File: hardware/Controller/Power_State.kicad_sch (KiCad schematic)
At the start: 24 parts, among them J3 ICSP Header, J7 UART DEBUG, Q2 NMOS, SW1 Button - User Interface, SW2 Button - Reset, U4 ATmega328-P, Y2 16 Mhz

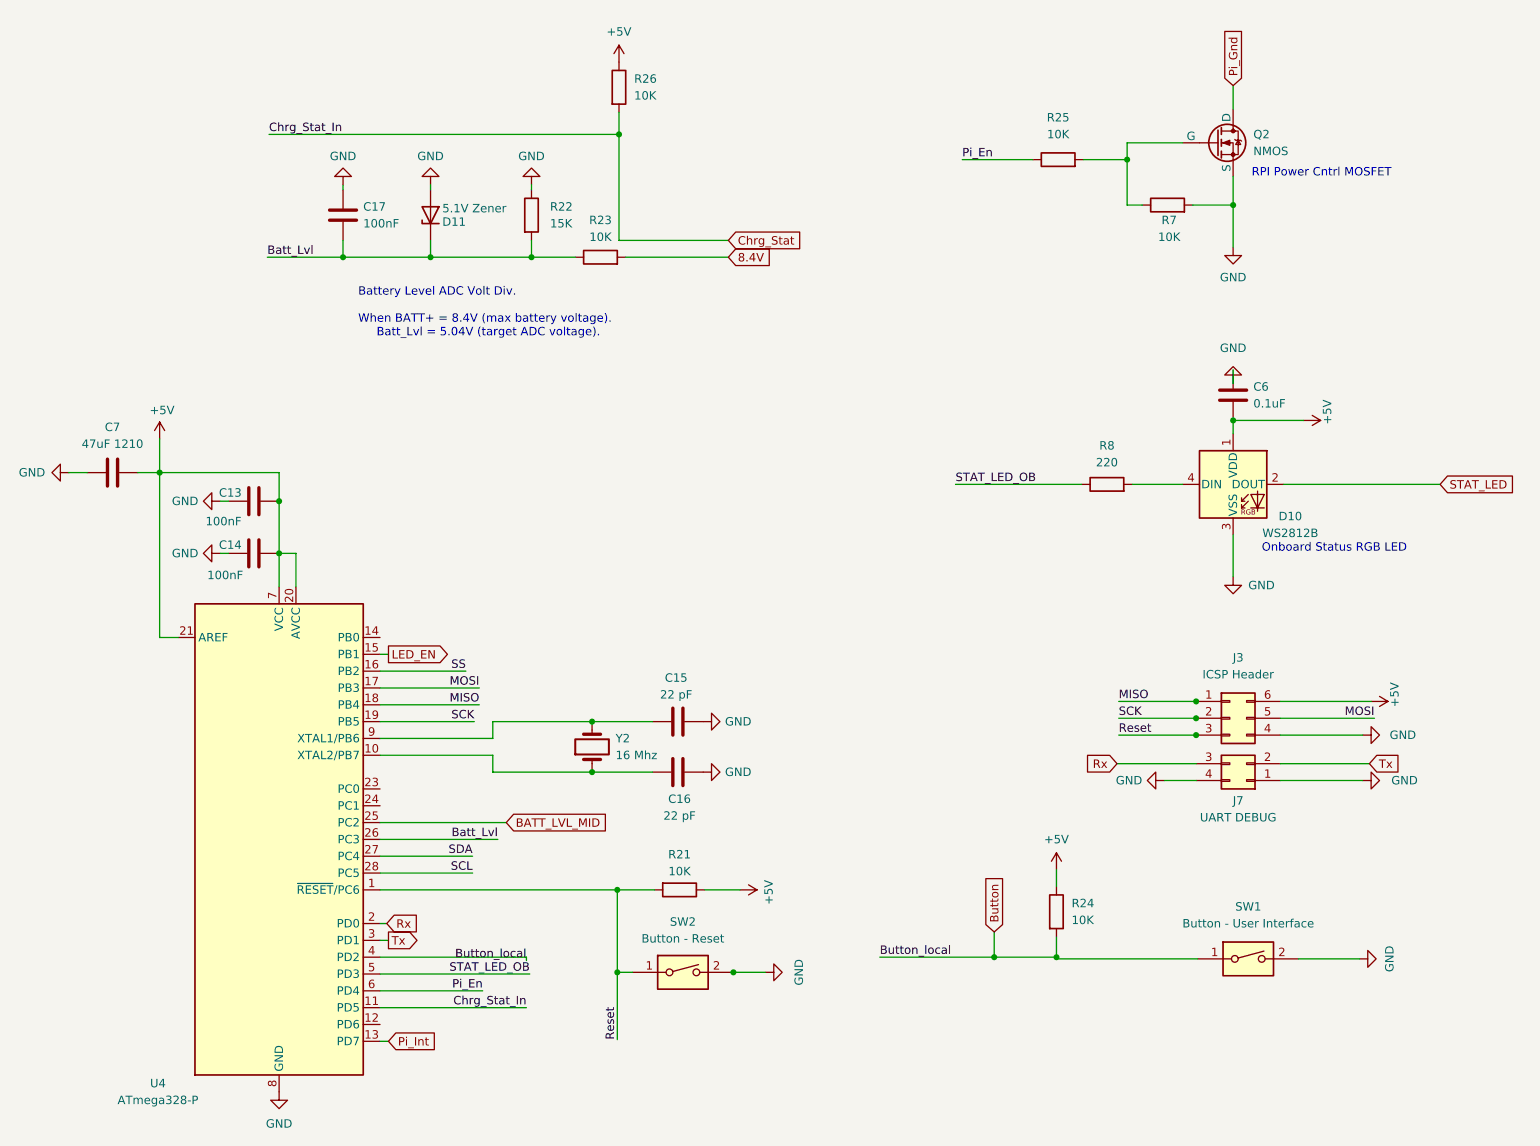
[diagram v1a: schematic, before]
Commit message: Hardware - Controller - Rev 0.3
* Consolidate various asset dirs into single symlinked directory.
* Fixes major flaw with previous atmega328 layout - wrong schematic symbol caused incorrect routing
* Use smaller crystal closer to mcu
* Add QR to silkscreen
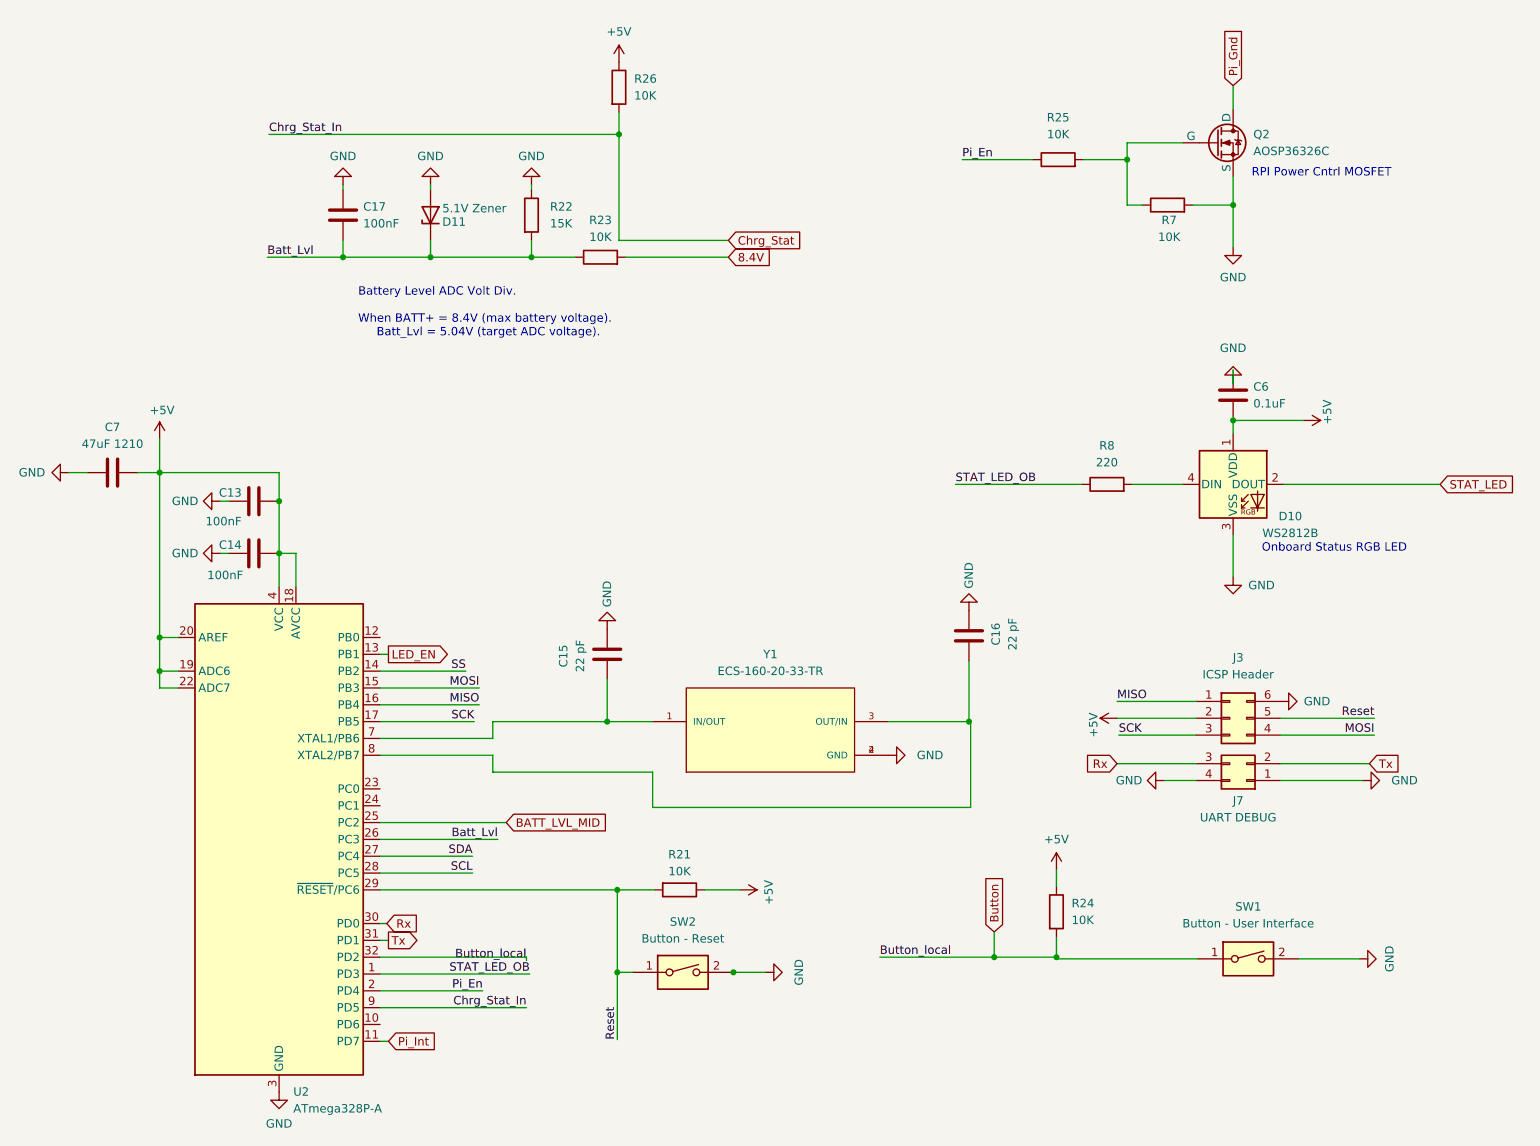
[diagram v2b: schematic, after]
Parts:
- removed U4: ATmega328-P, ATMEGA328-AU:QFP80P900X900X120-32N, symbol MCU_Microchip_ATmega:ATmega328-P
- removed Y2: 16 Mhz, Crystal - 16MHz ECS_160_20_5PX_TR:XTAL_ECS-160-20-5PX-TR, symbol Device:Crystal
- added U2: ATmega328P-A, Package_QFP:TQFP-32_7x7mm_P0.8mm, symbol MCU_Microchip_ATmega:ATmega328P-A
- added Y1: ECS-160-20-33-TR, ECS-160-20-33-TR:XTAL_ECS-160-20-33-TR, symbol ECS-160-20-33-TR:ECS-160-20-33-TR
- D11: footprint Diode_SMD:D_MiniMELF_Handsoldering -> Diode_SMD:D_SOD-323_HandSoldering
- Q2: value NMOS -> AOSP36326C; footprint FET - AOSP36326C:SOIC127P490X600X175-8N -> AOSP36326C:SOIC127P490X600X175-8N
- SW1, SW2: footprint Button - PTS815 Tactile SW:SW4_PTS815 SJM 250 SMTR LFS_CNK -> Button - PTS815:SW4_PTS815 SJM 250 SMTR LFS_CNK
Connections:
- net +5V: now also J3.2 (Pin_2), U2.18 (AVCC), U2.19 (ADC6), U2.20 (AREF), U2.22 (ADC7), U2.4 (VCC), U2.6 (VCC); no longer J3.6 (Pin_6)
- net BATT_LVL_MID: now also U2.25 (PC2)
- net Batt_Lvl: now also U2.26 (PC3)
- net Button: now also U2.32 (PD2)
- net Chrg_Stat: now also U2.9 (PD5)
- net GND: now also J3.6 (Pin_6), U2.21 (GND), U2.3 (GND), U2.5 (GND), Y1.2 (GND), Y1.4 (GND); no longer J3.4 (Pin_4)
- net LED_EN: now also U2.13 (PB1)
- net MISO: now also U2.16 (PB4)
- net MOSI: now also J3.4 (Pin_4), U2.15 (PB3); no longer J3.5 (Pin_5)
- net Pi_En: now also U2.2 (PD4)
- net Pi_Int: now also U2.11 (PD7)
- net Reset: now also J3.5 (Pin_5), U2.29 (~{RESET}/PC6); no longer J3.3 (Pin_3)
- net Rx: now also U2.30 (PD0)
- net SCK: now also J3.3 (Pin_3), U2.17 (PB5); no longer J3.2 (Pin_2)
- net SCL: now also U2.28 (PC5)
- net SDA: now also U2.27 (PC4)
- net SS: now also U2.14 (PB2)
- net STAT_LED_OB: now also U2.1 (PD3)
- net Tx: now also U2.31 (PD1)
- net at C16.1: now also U2.8 (XTAL2/PB7), Y1.3 (OUT/IN)
- net at C15.1: now also U2.7 (XTAL1/PB6), Y1.1 (IN/OUT)
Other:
- moved on the sheet: C15, C16
